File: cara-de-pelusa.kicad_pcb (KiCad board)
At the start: 2 copper layers, 30.9 x 34.2 mm, 23 parts, among them J1 Power bottom, J2 Stomp, J3 Power top, Q1 BC108, Q2 BC109

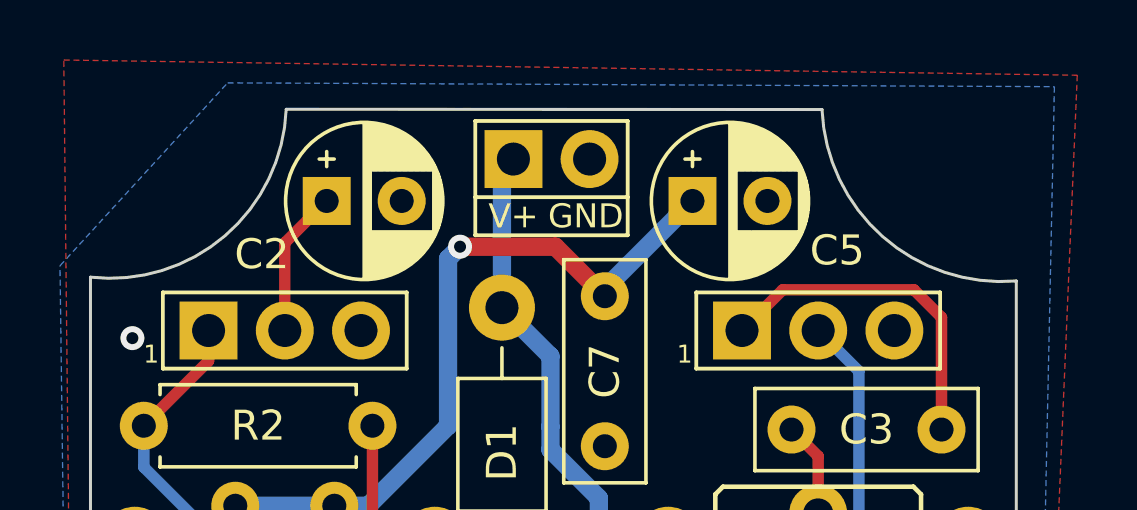
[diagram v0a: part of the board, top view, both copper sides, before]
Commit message: updated to KiCad 6.0
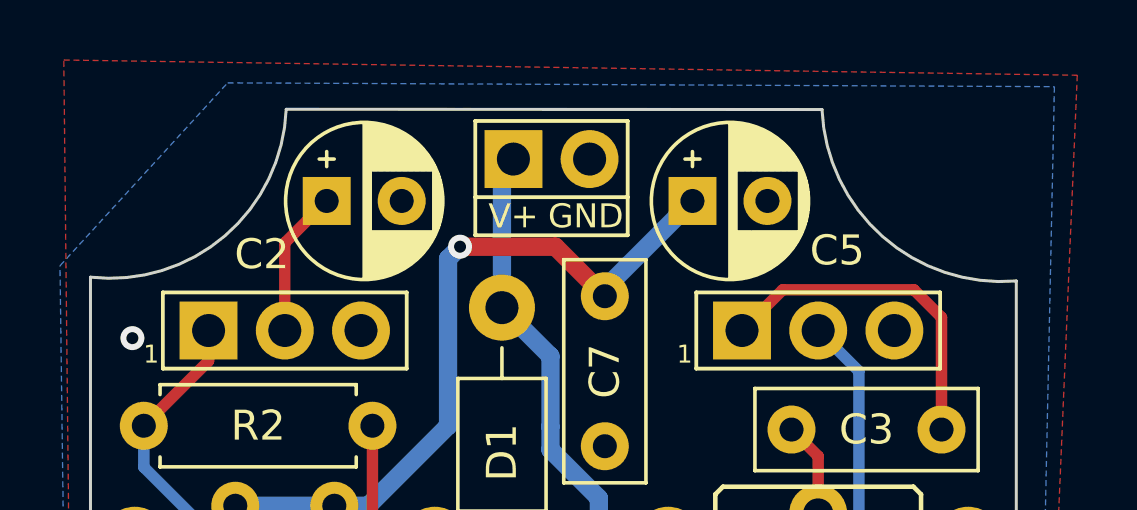
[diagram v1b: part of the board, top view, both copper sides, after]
